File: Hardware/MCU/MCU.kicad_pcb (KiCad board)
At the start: 4 copper layers, 75 x 100 mm, 34 parts, among them J1 spi0, J10 i2c1, J11 1778612, J12 i2c0, J2 i2s, J3 1778612, J5 1778612, J6 sp1, J7 sp2, J8 USB_C_Receptacle_USB2.0_16P, J9 1778612, SW1 SW_Push, SW2 SW_Push, U1 ESP32-S3-WROOM-1, U2 USBLC6-2P6

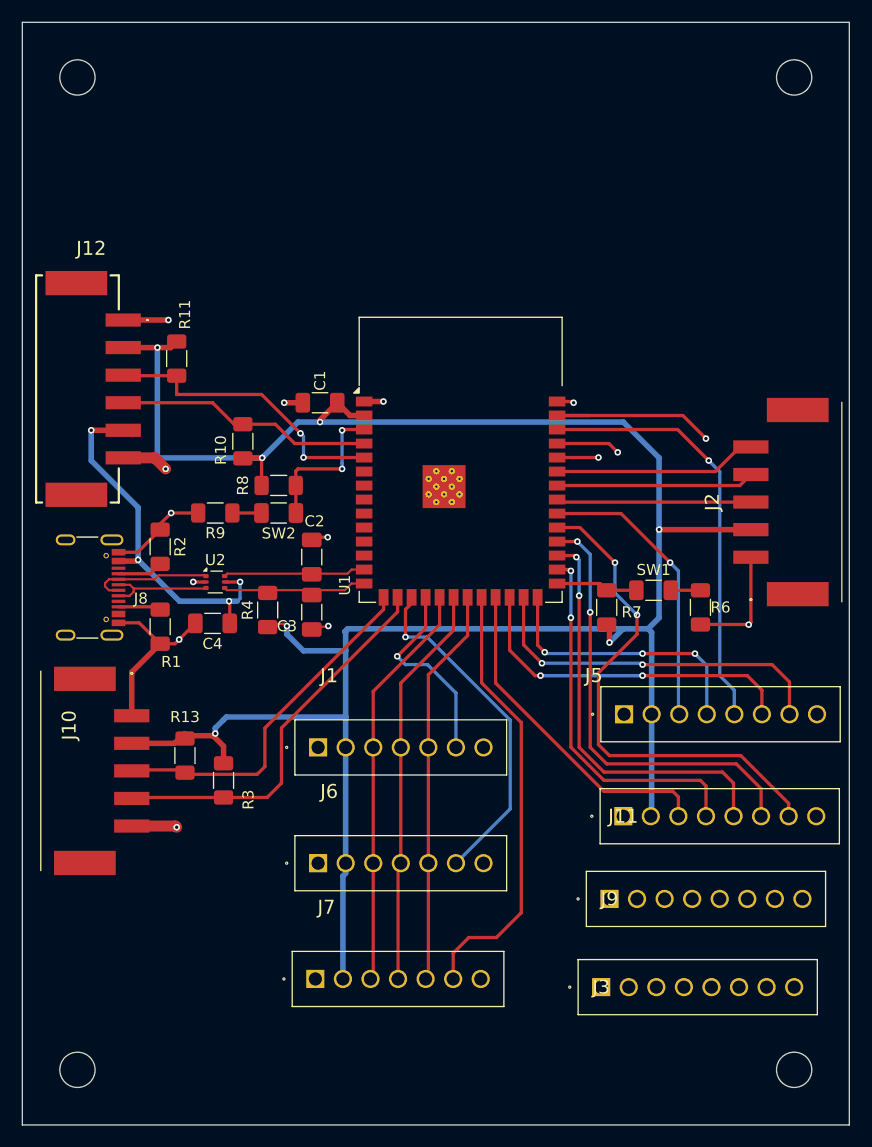
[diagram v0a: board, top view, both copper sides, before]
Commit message: updated traces en layout
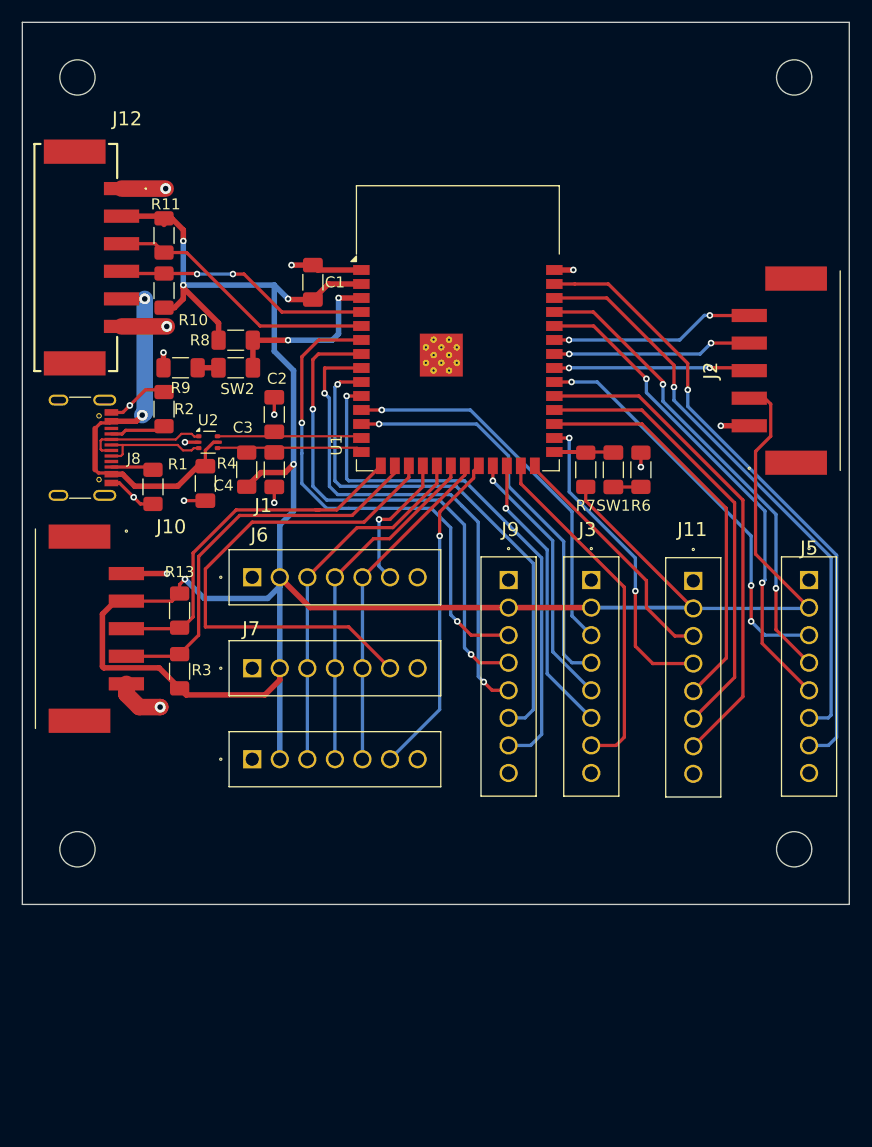
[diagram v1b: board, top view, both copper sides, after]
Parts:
- moved J3 36.9 mm to (147.6, 99.6), turned to -90 degrees
- moved J9 30.3 mm to (140.1, 99.6), turned to -90 degrees
- moved J11 22.3 mm to (156.8, 99.7), turned to -90 degrees
- moved J7 20.7 mm to (116.8, 115.8)
- moved J5 20.7 mm to (167.3, 99.6), turned to -90 degrees
- moved H3 20.0 mm to (166.0, 124.0)
- moved H4 20.0 mm to (101.0, 124.0)
- moved J6 18.7 mm to (116.8, 107.6)
- moved J1 16.5 mm to (116.8, 99.3)
- moved R10 15.4 mm to (108.8, 73.3)
- moved R8 13.7 mm to (115.3, 77.8)
- moved SW2 13.7 mm to (115.3, 80.3)
- moved R6 13.6 mm to (152.1, 89.6), turned to 90 degrees
- moved R9 13.5 mm to (110.3, 80.3)
- moved C2 13.4 mm to (118.8, 84.6)
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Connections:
- J11 pad 3: io21 -> io45
- J3 pad 3: io16 -> io18
- J3 pad 4: io17 -> io8
- J3 pad 5: io18 -> io21
- J3 pad 6: txd0 -> io47
- J3 pad 7: rxd0 -> io48
- J5 pad 4: io45 -> txd0
- J5 pad 5: io2 -> rxd0
- J5 pad 6: io47 -> io2
- J5 pad 7: io48 -> io1
- J9 pad 3: io1 -> io6
- J9 pad 4: io6 -> io7
- J9 pad 5: io7 -> io15
- J9 pad 6: io8 -> io16
- J9 pad 7: io15 -> io17
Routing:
- net io17: track 0.00 -> 48.9 mm, vias 0 -> 1
- net io16: track 0.00 -> 48.0 mm, vias 0 -> 1
- net io7: track 0.00 -> 47.0 mm, vias 0 -> 2
- net io6: track 0.00 -> 46.6 mm, vias 0 -> 2
- net io15: track 0.00 -> 46.4 mm, vias 0 -> 2
- net rxd0: track 3.75 -> 44.9 mm, vias 1 -> 2
- net io1: track 17.4 -> 57.4 mm
- net txd0: track 5.83 -> 43.5 mm, vias 1 -> 2
- net io8: track 0.00 -> 37.6 mm, vias 0 -> 1
- net io18: track 0.00 -> 35.0 mm, vias 0 -> 1
- net ss1: track 31.5 -> 46.5 mm, vias 1 -> 0
- net io2: track 38.9 -> 53.1 mm
- net GND: track 49.6 -> 38.4 mm, vias 10 -> 13
- net io39: track 26.2 -> 37.2 mm, vias 1 -> 3
- net ss2: track 40.1 -> 29.9 mm, vias 0 -> 1
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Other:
- board size 75 x 100 mm -> 75 x 80 mm

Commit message: mierenneukerij
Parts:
- moved J3 1.58 mm to (149.2, 99.6)
- moved J11 1.42 mm to (158.3, 99.6)
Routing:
- net +3.3V: track 218.8 -> 221.0 mm
- net io47: track 26.1 -> 27.7 mm
- net io21: track 24.1 -> 25.6 mm
- net io35: track 28.6 -> 30.1 mm
- net io45: track 22.4 -> 23.8 mm
- net io48: track 31.8 -> 30.7 mm
- net ss0: track 13.3 -> 12.4 mm
- net GND: track 38.4 -> 37.5 mm
- net io38: track 45.2 -> 44.4 mm
- net io37: track 41.0 -> 40.3 mm
- net io36: track 36.6 -> 35.9 mm
- net txd0: track 43.5 -> 44.0 mm

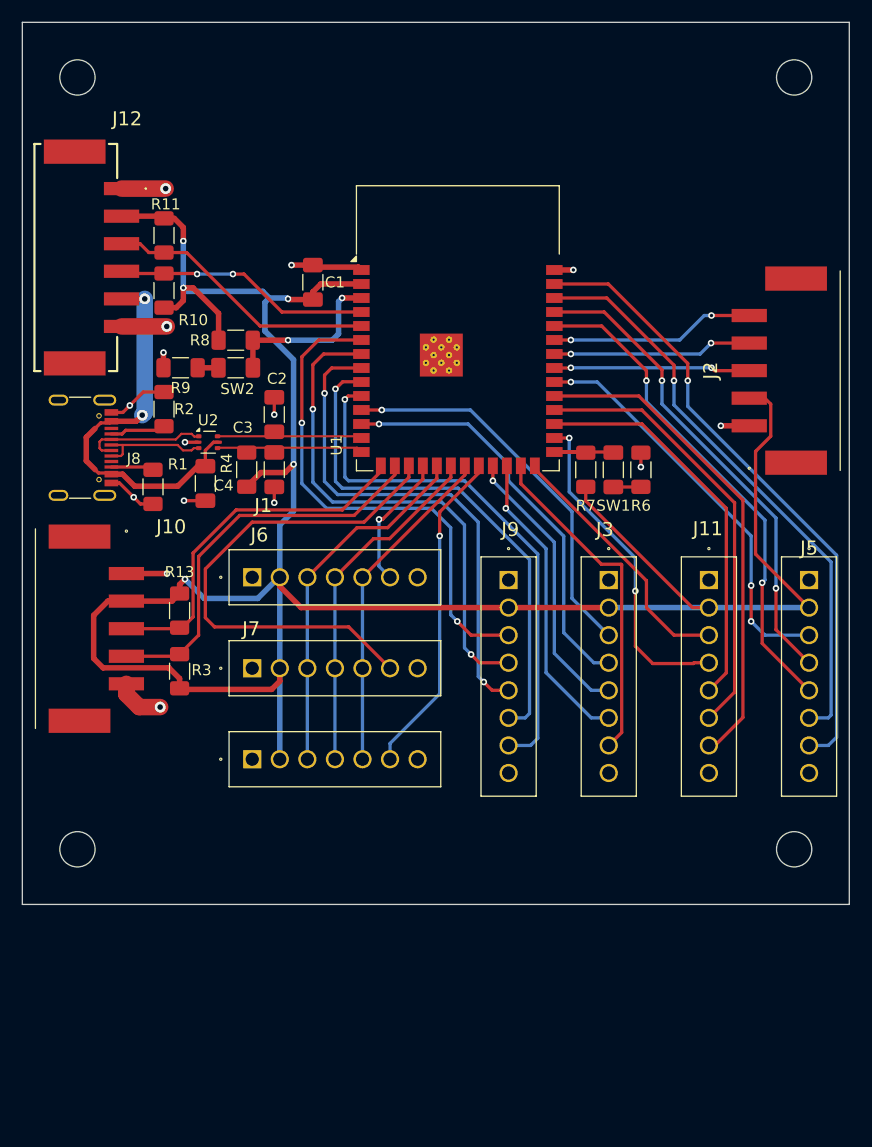
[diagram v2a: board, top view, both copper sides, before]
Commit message: schematische tekening geordend
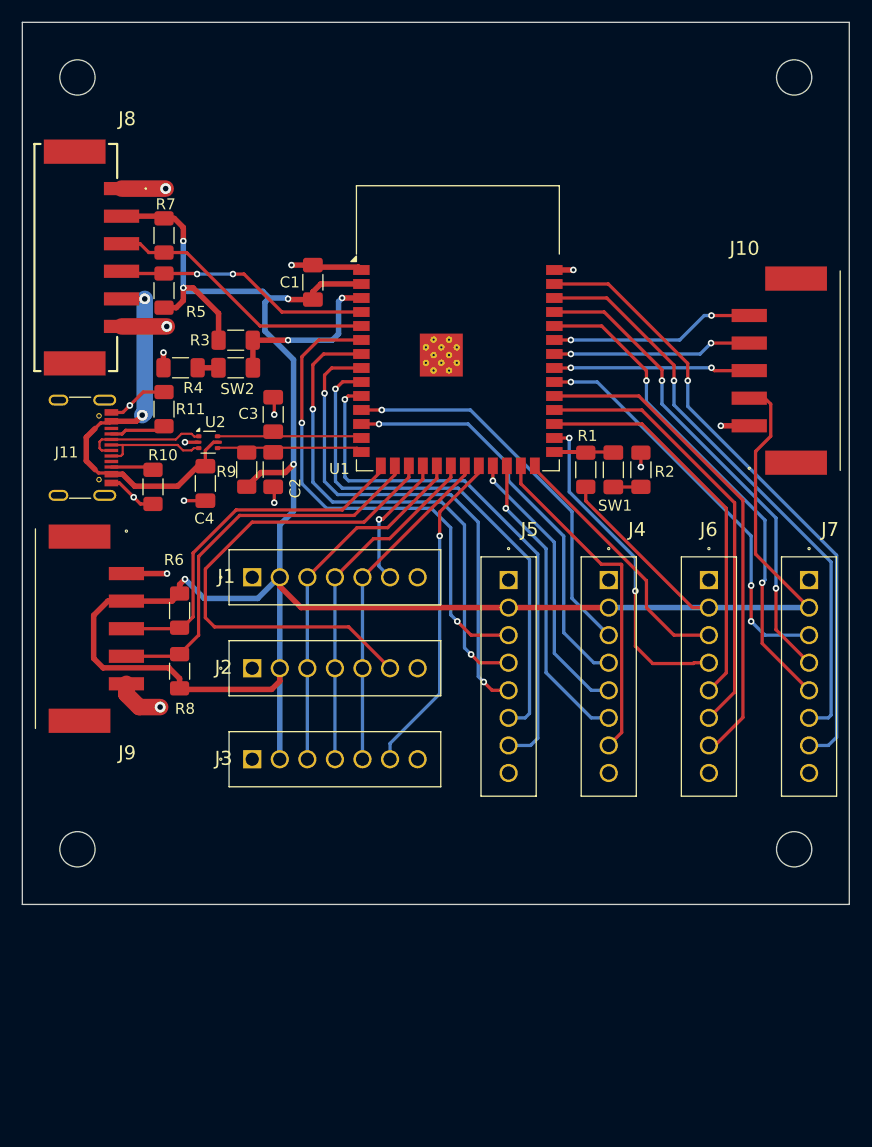
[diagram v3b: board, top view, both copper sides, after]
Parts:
- moved C3 5.01 mm to (118.8, 84.6), turned to -90 degrees
- moved C2 4.99 mm to (118.8, 89.6), turned to 90 degrees
- renumbered H4 to H1, H3 to H2, H2 to H3, H1 to H4, J2 to J10, J8 to J11, J6 to J2, J7 to J3, J3 to J4, J9 to J5, J11 to J6, J5 to J7, J12 to J8, J10 to J9, R7 to R1, R1 to R10, R2 to R11, R6 to R2, R8 to R3, R9 to R4, R10 to R5, R13 to R6, R11 to R7, R3 to R8, R4 to R9
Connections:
- C2 pad 2: - -> +
- C3 pad 2: + -> -

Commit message: added usb weerstanden
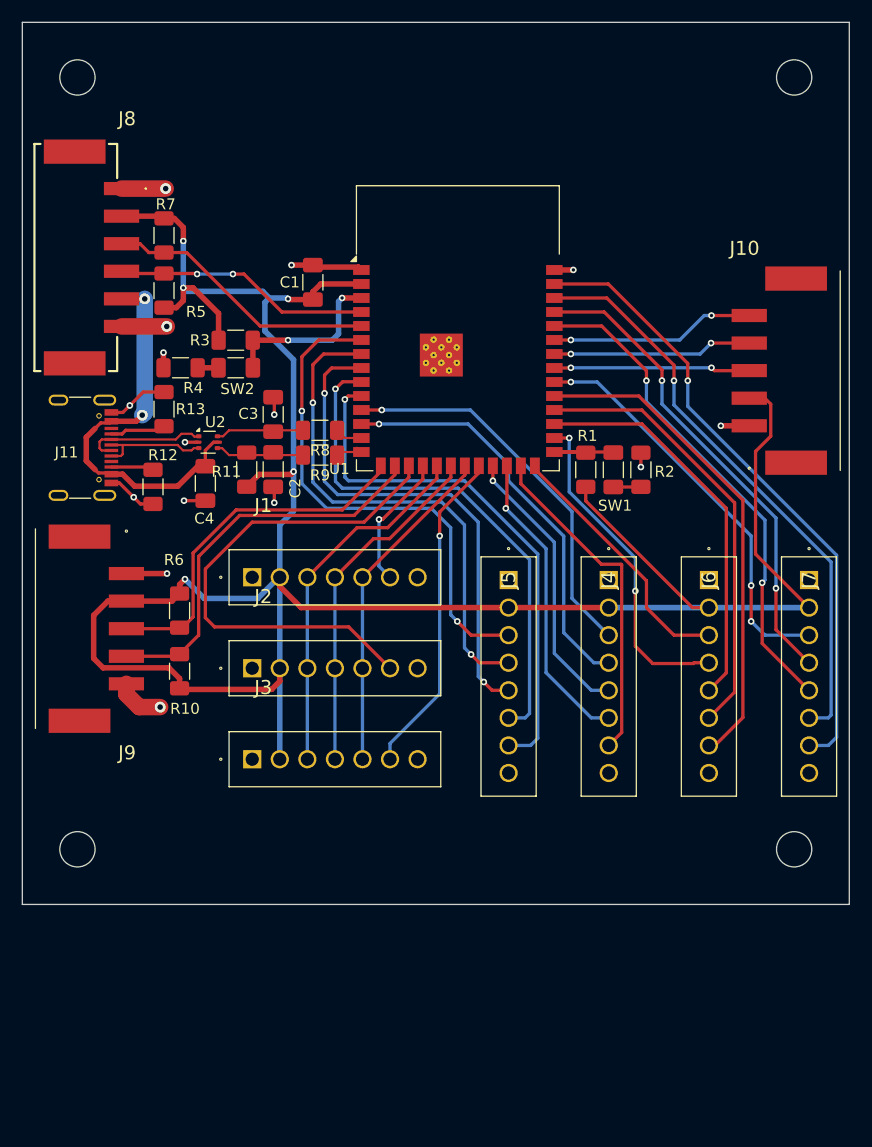
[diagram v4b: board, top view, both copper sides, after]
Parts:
- added R8: 0, Resistor_SMD:R_1206_3216Metric_Pad1.30x1.75mm_HandSolder, F.Cu at (123.0, 86.0)
- added R9: 0, Resistor_SMD:R_1206_3216Metric_Pad1.30x1.75mm_HandSolder, F.Cu at (123.0, 88.2)
- renumbered R8 to R10, R9 to R11, R10 to R12, R11 to R13
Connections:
- U1 pad 13: - -> Net-(U1-USB_D-)
- U1 pad 14: + -> Net-(U1-USB_D+)
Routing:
- net +: track 13.2 -> 8.07 mm
- net -: track 13.1 -> 7.97 mm
- net Net-(U1-USB_D+): track 0.00 -> 2.87 mm
- net Net-(U1-USB_D-): track 0.00 -> 2.71 mm

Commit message: edited footprint buttons
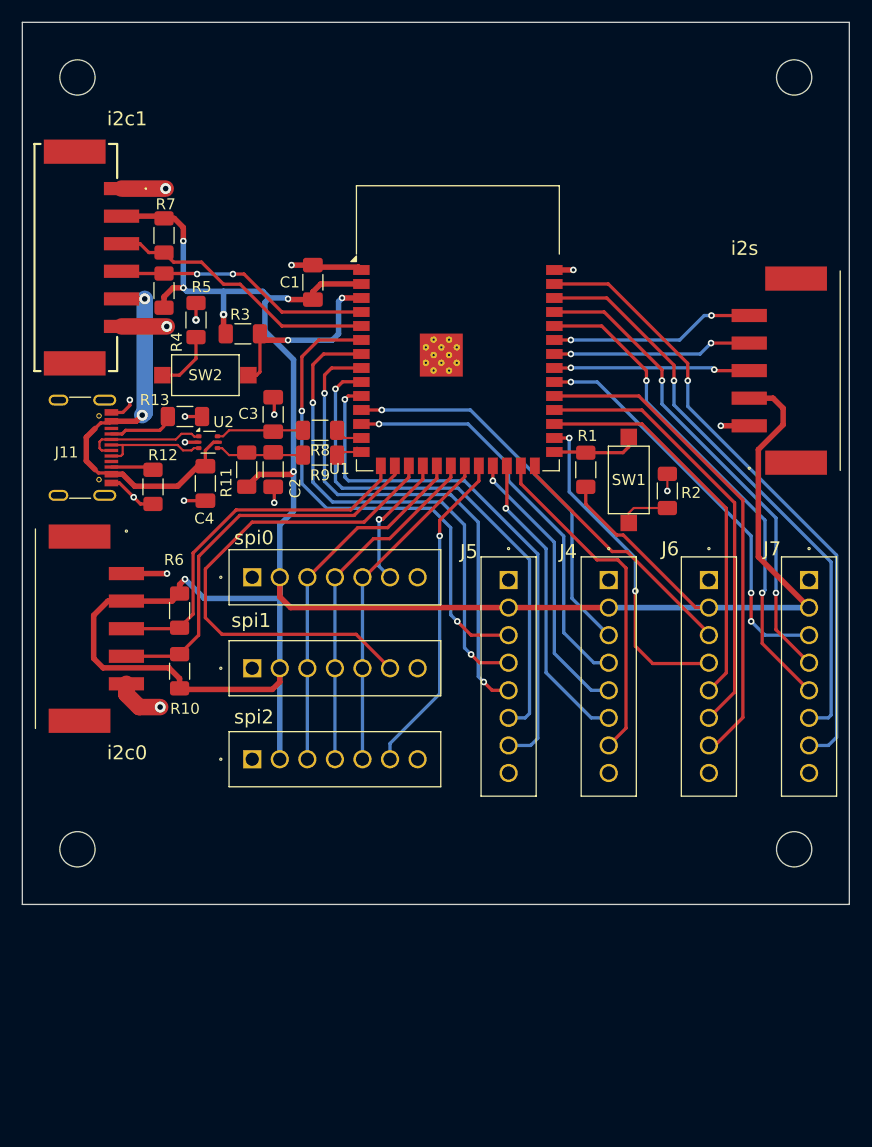
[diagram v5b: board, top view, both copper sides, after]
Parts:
- SW1, SW2: footprint Capacitor_SMD:C_1206_3216Metric_Pad1.33x1.80mm_HandSolder -> Button_Switch_SMD:SW_SPST_CK_RS282G05A3
- moved R4 4.55 mm to (111.8, 76.0), turned to 90 degrees
- moved R2 3.07 mm to (154.5, 91.5)
- moved SW2 2.83 mm to (112.6, 81.0)
- moved R13 2.01 mm to (110.8, 84.8), turned to 180 degrees
- moved SW1 1.68 mm to (151.0, 90.5)
- moved R3 0.87 mm to (116.0, 77.2)
- renumbered J9 to i2c0, J8 to i2c1, J10 to i2s, J1 to spi0, J2 to spi1, J3 to spi2
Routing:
- net Net-(R4-Pad1): track 1.89 -> 5.72 mm
- net Net-(R2-Pad1): track 2.51 -> 4.59 mm
- net reset: track 15.7 -> 17.5 mm
- net GND: track 37.6 -> 36.4 mm, vias 13 -> 14
- net +3.3V: track 220.7 -> 221.0 mm, vias 5 -> 6

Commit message: silkscreen aangepast
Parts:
- moved R4 0.25 mm to (112.0, 76.0)
- renumbered J11 to usb-c
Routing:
- net ss1: track 46.0 -> 43.8 mm
- net sda0: track 33.4 -> 34.6 mm
- net +5Vout: track 36.4 -> 35.4 mm, vias 2 -> 3
- net scl0: track 36.2 -> 35.5 mm

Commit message: Update MCU.kicad_pcb
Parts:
- renumbered SW1 to BOOT, J5 to GPIO0, J4 to GPIO1, J6 to GPIO2, J7 to GPIO3, i2c0 to I2C0, i2c1 to I2C1, i2s to I2S, SW2 to RESET, spi0 to SPI0, spi1 to SPI1, spi2 to SPI2
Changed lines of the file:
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@@
 		(descr "https://www.mouser.com/ds/2/60/RS-282G05A-SM_RT-1159762.pdf")
 		(tags "SPST button tactile switch")
-		(property "Reference" "SW2"
-			(at 0 0 0)
+		(property "Reference" "RESET"
+			(at -7.4 0 0)
 			(layer "F.SilkS")
 			(effects
@@
 		(descr "https://www.mouser.com/ds/2/60/RS-282G05A-SM_RT-1159762.pdf")
 		(tags "SPST button tactile switch")
-		(property "Reference" "SW1"
-			(at 0 0 180)
+		(property "Reference" "BOOT"
+			(at -3.5 -4 180)
 			(layer "F.SilkS")
 			(effects
@@
 		(descr "1778609")
 		(tags "Connector")
-		(property "Reference" "spi1"
-			(at 1.65 -4.33 0)
+		(property "Reference" "SPI1"
+			(at 1.65 -3.38 0)
 			(layer "F.SilkS")
 			(effects
@@
 		(descr "1814951-7")
 		(tags "Connector")
-		(property "Reference" "i2c1"
+		(property "Reference" "I2C1"
 			(at -12.58 -3.65 0)
 			(layer "F.SilkS")
@@
 		(descr "1778612")
 		(tags "Connector")
-		(property "Reference" "J5"
-			(at -2.58 3.6 180)
+		(property "Reference" "GPIO0"
+			(at -2.78 3.3 180)
 			(layer "F.SilkS")
 			(effects
@@
 		(descr "1778609")
 		(tags "Connector")
-		(property "Reference" "spi2"
-			(at 1.9 -4.08 0)
+		(property "Reference" "SPI2"
+			(at 1.9 -3.43 0)
 			(layer "F.SilkS")
 			(effects
@@
 		(descr "1778612")
 		(tags "Connector")
-		(property "Reference" "J7"
-			(at -2.83 3.35 0)
+		(property "Reference" "GPIO3"
+			(at -2.83 2.95 0)
 			(layer "F.SilkS")
 			(effects
@@
 		(descr "1778612")
 		(tags "Connector")
-		(property "Reference" "J6"
-			(at -2.83 3.516666 0)
+		(property "Reference" "GPIO2"
+			(at -2.83 3.266666 0)
 			(layer "F.SilkS")
 			(effects
@@
 		(descr "1814948")
 		(tags "Connector")
-		(property "Reference" "i2s"
+		(property "Reference" "I2S"
 			(at 11.09 -0.425 180)
 			(layer "F.SilkS")
@@
 		(descr "1814948")
 		(tags "Connector")
-		(property "Reference" "i2c0"
+		(property "Reference" "I2C0"
 			(at 11.2575 -0.0625 180)
 			(layer "F.SilkS")
@@
 		(descr "1778609")
 		(tags "Connector")
-		(property "Reference" "spi0"
-			(at 1.65 -4.08 0)
+		(property "Reference" "SPI0"
+			(at 1.75 -3.33 0)
 			(layer "F.SilkS")
 			(effects
@@
 		(descr "1778612")
 		(tags "Connector")
-		(property "Reference" "J4"
-			(at -2.58 3.683333 0)
+		(property "Reference" "GPIO1"
+			(at -2.78 3.383333 0)
 			(layer "F.SilkS")
 			(effects
@@
 	)
 	(segment
+		(start 104.075 90.78)
+		(end 105.365 92.07)
+		(width 0.3)
+		(layer "F.Cu")
+		(net 1)
+	)
+	(segment
 		(start 159.35 85.59)
 		(end 161.925 85.59)
@@
 	)
 	(segment
-		(start 104.075 90.78)
-		(end 104.81 90.78)
-		(width 0.3)
-		(layer "F.Cu")
-		(net 1)
-	)
-	(segment
 		(start 106.71 92.68)
 		(end 107.85 92.68)
@@
 	)
 	(segment
-		(start 104.81 90.78)
-		(end 106.1 92.07)
-		(width 0.3)
+		(start 105 64.08)
+		(end 109 64.08)
+		(width 1.5)
 		(layer "F.Cu")
 		(net 1)
 	)
 	(segment
-		(start 105 64.08)
-		(end 109 64.08)
-		(width 1.5)
+		(start 105.365 92.07)
+		(end 106.1 92.07)
+		(width 0.3)
 		(layer "F.Cu")
 		(net 1)
@@
 	(via
 		(at 109 64.08)
-		(size 1)
-		(drill 0.5)
+		(size 1.5)
+		(drill 1)
 		(layers "F.Cu" "B.Cu")
 		(net 1)
@@
 	(via
 		(at 106.875 84.625)
-		(size 1)
-		(drill 0.5)
+		(size 1.5)
+		(drill 1)
 		(layers "F.Cu" "B.Cu")
 		(net 5)
@@
 	(via
 		(at 107.1 74.08)
-		(size 1)
-		(drill 0.5)
+		(size 1.3)
+		(drill 0.8)
 		(layers "F.Cu" "B.Cu")
 		(net 5)
@@
 	(via
 		(at 106 90.75)
-		(size 1)
-		(drill 0.5)
+		(size 1.2)
+		(drill 0.8)
 		(layers "F.Cu" "B.Cu")
 		(net 5)
@@
 	(via
 		(at 109.1 76.58)
-		(size 1)
-		(drill 0.5)
+		(size 1.5)
+		(drill 1)
 		(layers "F.Cu" "B.Cu")
 		(net 11)
@@
 	(via
 		(at 108.5 111.1025)
-		(size 1)
-		(drill 0.5)
+		(size 1.5)
+		(drill 1)
 		(layers "F.Cu" "B.Cu")
 		(net 11)
